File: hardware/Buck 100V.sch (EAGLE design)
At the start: 31 parts, among them M1 SI3430DV, M2 SI5435BDC, Q1 FMMT625, Q2 FMMT723, U1 LT3756EMSE

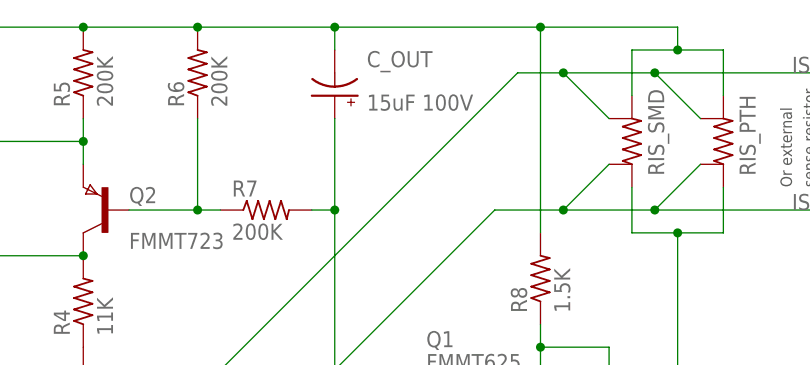
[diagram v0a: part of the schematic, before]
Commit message: Some progress on layout and routing.
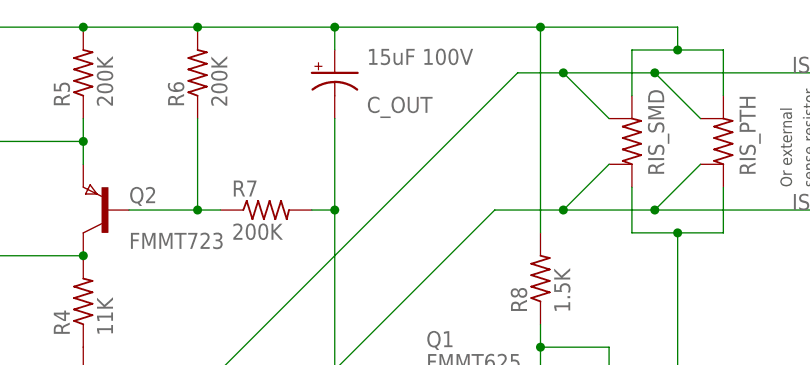
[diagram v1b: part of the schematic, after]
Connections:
- net LED_C: now also C_OUT.-; no longer C_OUT.+
- net V+: now also C_OUT.+; no longer C_OUT.-
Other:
- moved on the sheet: C_OUT
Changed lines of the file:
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@@
 <instance part="JH" gate="1" x="182.88" y="50.8" rot="R180"/>
 <instance part="JL" gate="1" x="182.88" y="22.86" rot="R180"/>
-<instance part="C_OUT" gate="G$1" x="66.04" y="55.88" smashed="yes" rot="R180">
-<attribute name="NAME" x="69.596" y="59.055" size="1.778" layer="95"/>
-<attribute name="VALUE" x="69.596" y="54.229" size="1.778" layer="96"/>
+<instance part="C_OUT" gate="G$1" x="66.04" y="58.42" smashed="yes">
+<attribute name="NAME" x="69.596" y="53.975" size="1.778" layer="95"/>
+<attribute name="VALUE" x="69.596" y="59.309" size="1.778" layer="96"/>
 </instance>
 <instance part="RIS_SMD" gate="G$1" x="99.06" y="50.8" rot="R90"/>
@@
 <wire x1="104.14" y1="63.5" x2="88.9" y2="63.5" width="0.1524" layer="91"/>
 <wire x1="88.9" y1="63.5" x2="66.04" y2="63.5" width="0.1524" layer="91"/>
+<junction x="50.8" y="63.5"/>
 <wire x1="66.04" y1="63.5" x2="50.8" y2="63.5" width="0.1524" layer="91"/>
-<junction x="50.8" y="63.5"/>
-<wire x1="66.04" y1="60.96" x2="66.04" y2="63.5" width="0.1524" layer="91"/>
-<junction x="66.04" y="63.5"/>
 <wire x1="99.06" y1="60.96" x2="104.14" y2="60.96" width="0.1524" layer="91"/>
 <wire x1="104.14" y1="60.96" x2="104.14" y2="63.5" width="0.1524" layer="91"/>
@@
 <wire x1="-58.42" y1="58.42" x2="-58.42" y2="63.5" width="0.1524" layer="91"/>
 <junction x="-58.42" y="63.5"/>
-<pinref part="C_OUT" gate="G$1" pin="-"/>
 <pinref part="RIS_PTH" gate="G$1" pin="2"/>
 <wire x1="109.22" y1="55.88" x2="109.22" y2="60.96" width="0.1524" layer="91"/>
 <pinref part="RIS_SMD" gate="G$1" pin="2"/>
 <wire x1="99.06" y1="55.88" x2="99.06" y2="60.96" width="0.1524" layer="91"/>
+<pinref part="C_OUT" gate="G$1" pin="+"/>
+<wire x1="66.04" y1="60.96" x2="66.04" y2="63.5" width="0.1524" layer="91"/>
+<junction x="66.04" y="63.5"/>
 </segment>
 <segment>
@@
 <wire x1="66.04" y1="43.18" x2="63.5" y2="43.18" width="0.1524" layer="91"/>
 <junction x="104.14" y="-2.54"/>
+<pinref part="C_OUT" gate="G$1" pin="-"/>
 <wire x1="66.04" y1="53.34" x2="66.04" y2="43.18" width="0.1524" layer="91"/>
 <junction x="66.04" y="43.18"/>
-<pinref part="C_OUT" gate="G$1" pin="+"/>
-</segment>
-<segment>
+</segment>
+<segment>

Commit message: Missed from previous commit.
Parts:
- added U$1: OSHW-LOGOS, SparkFun-Aesthetics:OSHW-LOGOS
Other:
- note added: "100V LED Buck Driver"
- note added: "DC Labs"
- note added: "www.danielcasner.org"
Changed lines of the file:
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@@
 <layer number="48" name="Document" color="7" fill="1" visible="no" active="no"/>
 <layer number="49" name="Reference" color="7" fill="1" visible="no" active="no"/>
+<layer number="50" name="dxf" color="7" fill="1" visible="no" active="no"/>
 <layer number="51" name="tDocu" color="7" fill="1" visible="no" active="no"/>
 <layer number="52" name="bDocu" color="7" fill="1" visible="no" active="no"/>
+<layer number="53" name="tGND_GNDA" color="7" fill="9" visible="no" active="no"/>
+<layer number="54" name="bGND_GNDA" color="1" fill="9" visible="no" active="no"/>
+<layer number="56" name="wert" color="7" fill="1" visible="no" active="no"/>
 <layer number="91" name="Nets" color="2" fill="1" visible="yes" active="yes"/>
 <layer number="92" name="Busses" color="1" fill="1" visible="yes" active="yes"/>
@@
 <layer number="97" name="Info" color="7" fill="1" visible="yes" active="yes"/>
 <layer number="98" name="Guide" color="6" fill="1" visible="yes" active="yes"/>
+<layer number="100" name="Muster" color="7" fill="1" visible="no" active="no"/>
+<layer number="101" name="Patch_Top" color="12" fill="4" visible="no" active="yes"/>
+<layer number="102" name="Vscore" color="7" fill="1" visible="no" active="yes"/>
+<layer number="103" name="tMap" color="7" fill="1" visible="no" active="yes"/>
+<layer number="104" name="Name" color="16" fill="1" visible="no" active="yes"/>
+<layer number="105" name="tPlate" color="7" fill="1" visible="no" active="yes"/>
+<layer number="106" name="bPlate" color="7" fill="1" visible="no" active="yes"/>
+<layer number="107" name="Crop" color="7" fill="1" visible="no" active="yes"/>
+<layer number="116" name="Patch_BOT" color="9" fill="4" visible="no" active="yes"/>
+<layer number="121" name="_tsilk" color="7" fill="1" visible="no" active="yes"/>
+<layer number="122" name="_bsilk" color="7" fill="1" visible="no" active="yes"/>
+<layer number="125" name="_tNames" color="7" fill="1" visible="no" active="yes"/>
+<layer number="144" name="Drill_legend" color="7" fill="1" visible="no" active="yes"/>
+<layer number="151" name="HeatSink" color="7" fill="1" visible="no" active="yes"/>
+<layer number="200" name="200bmp" color="1" fill="10" visible="no" active="yes"/>
+<layer number="201" name="201bmp" color="2" fill="10" visible="no" active="yes"/>
+<layer number="202" name="202bmp" color="3" fill="10" visible="no" active="yes"/>
+<layer number="203" name="203bmp" color="4" fill="10" visible="no" active="yes"/>
+<layer number="204" name="204bmp" color="5" fill="10" visible="no" active="yes"/>
+<layer number="205" name="205bmp" color="6" fill="10" visible="no" active="yes"/>
+<layer number="206" name="206bmp" color="7" fill="10" visible="no" active="yes"/>
+<layer number="207" name="207bmp" color="8" fill="10" visible="no" active="yes"/>
+<layer number="208" name="208bmp" color="9" fill="10" visible="no" active="yes"/>
+<layer number="209" name="209bmp" color="7" fill="1" visible="no" active="yes"/>
+<layer number="210" name="210bmp" color="7" fill="1" visible="no" active="yes"/>
+<layer number="211" name="211bmp" color="7" fill="1" visible="no" active="yes"/>
+<layer number="212" name="212bmp" color="7" fill="1" visible="no" active="yes"/>
+<layer number="213" name="213bmp" color="7" fill="1" visible="no" active="yes"/>
+<layer number="214" name="214bmp" color="7" fill="1" visible="no" active="yes"/>
+<layer number="215" name="215bmp" color="7" fill="1" visible="no" active="yes"/>
+<layer number="216" name="216bmp" color="7" fill="1" visible="no" active="yes"/>
+<layer number="217" name="217bmp" color="18" fill="1" visible="no" active="no"/>
+<layer number="218" name="218bmp" color="19" fill="1" visible="no" active="no"/>
+<layer number="219" name="219bmp" color="20" fill="1" visible="no" active="no"/>
+<layer number="220" name="220bmp" color="21" fill="1" visible="no" active="no"/>
+<layer number="221" name="221bmp" color="22" fill="1" visible="no" active="no"/>
+<layer number="222" name="222bmp" color="23" fill="1" visible="no" active="no"/>
+<layer number="223" name="223bmp" color="24" fill="1" visible="no" active="no"/>
+<layer number="224" name="224bmp" color="25" fill="1" visible="no" active="no"/>
+<layer number="250" name="Descript" color="3" fill="1" visible="no" active="no"/>
+<layer number="251" name="SMDround" color="12" fill="11" visible="no" active="no"/>
+<layer number="254" name="cooling" color="7" fill="1" visible="no" active="yes"/>
 </layers>
 <schematic xreflabel="%F%N/%S.%C%R" xrefpart="/%S.%C%R">
@@
 <part name="RIS_SMD" library="LED-drivers" deviceset="R-KELVIN" device="R2512"/>
 <part name="RIS_PTH" library="LED-drivers" deviceset="R-KELVIN" device="0204/7"/>
+<part name="U$1" library="SparkFun-Aesthetics" deviceset="OSHW-LOGO" device="S"/>
 </parts>
 <sheets>
@@
 <text x="119.38" y="45.72" size="1.27" layer="97" rot="R90">sense resistor</text>
 <text x="111.76" y="2.54" size="1.778" layer="97">External LED string</text>
+<text x="144.78" y="-12.7" size="2.54" layer="97">DC Labs</text>
+<text x="144.78" y="-17.78" size="2.54" layer="97">100V LED Buck Driver</text>
+<text x="144.78" y="-22.86" size="2.54" layer="97">www.danielcasner.org</text>
 </plain>
 <instances>
@@
 <instance part="RIS_SMD" gate="G$1" x="99.06" y="50.8" rot="R90"/>
 <instance part="RIS_PTH" gate="G$1" x="109.22" y="50.8" rot="R90"/>
+<instance part="U$1" gate="G$1" x="160.02" y="-33.02"/>
 </instances>
 <busses>
